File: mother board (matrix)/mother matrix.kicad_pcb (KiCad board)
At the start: 4 copper layers, 83.5 x 102.9 mm, 174 parts, among them J1 POWER, J2 DATA IN, J3 DATA OUT, J4 Serial_BUS, J5 OUTPUT, J6 INPUT, Q1 PMV45EN2R, Q10 PMV45EN2R, Q2 PMV45EN2R, Q3 PMV45EN2R, Q4 PMV45EN2R, Q5 PMV45EN2R, Q6 PMV45EN2R, Q7 PMV45EN2R, Q8 PMV45EN2R, Q9 PMV45EN2R, U1 SM16206, U2 SM16206, U3 SM16206

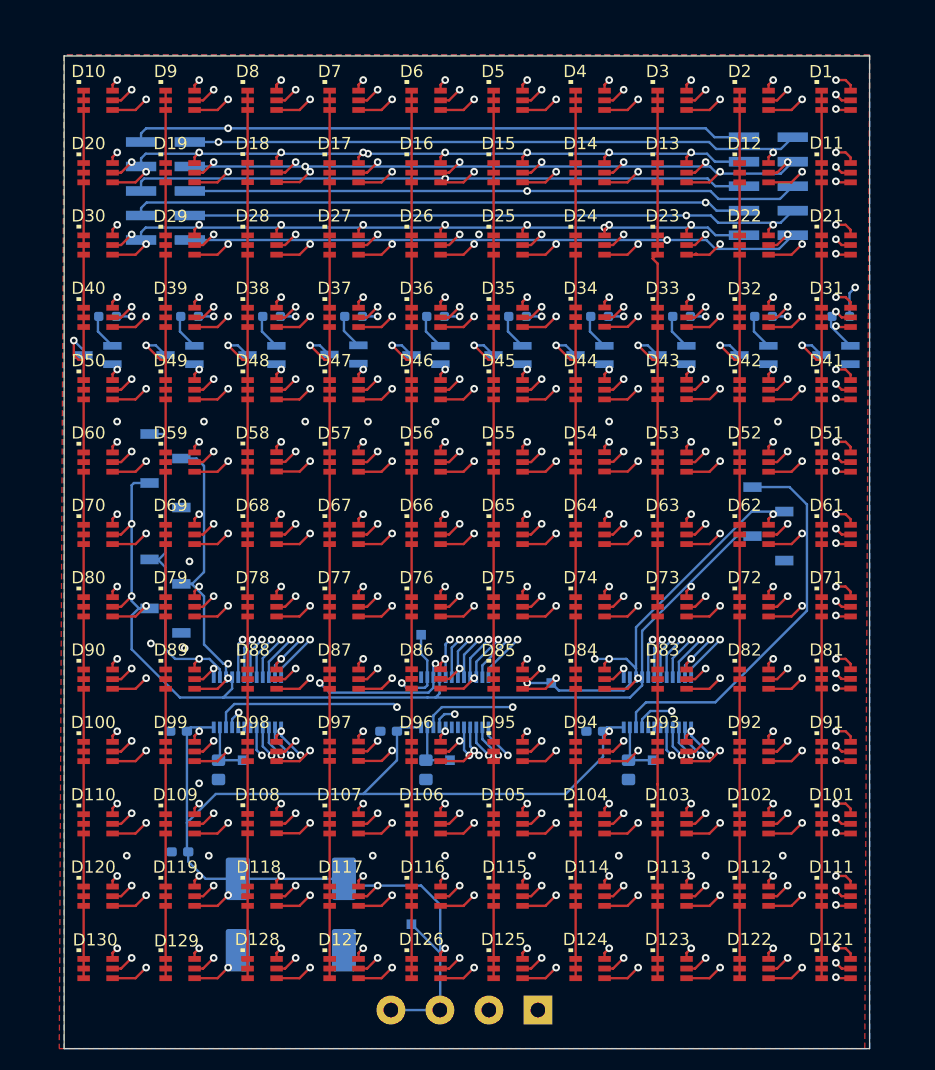
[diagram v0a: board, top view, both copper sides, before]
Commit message: Fixed GND planes and rerouted bottom layer signals
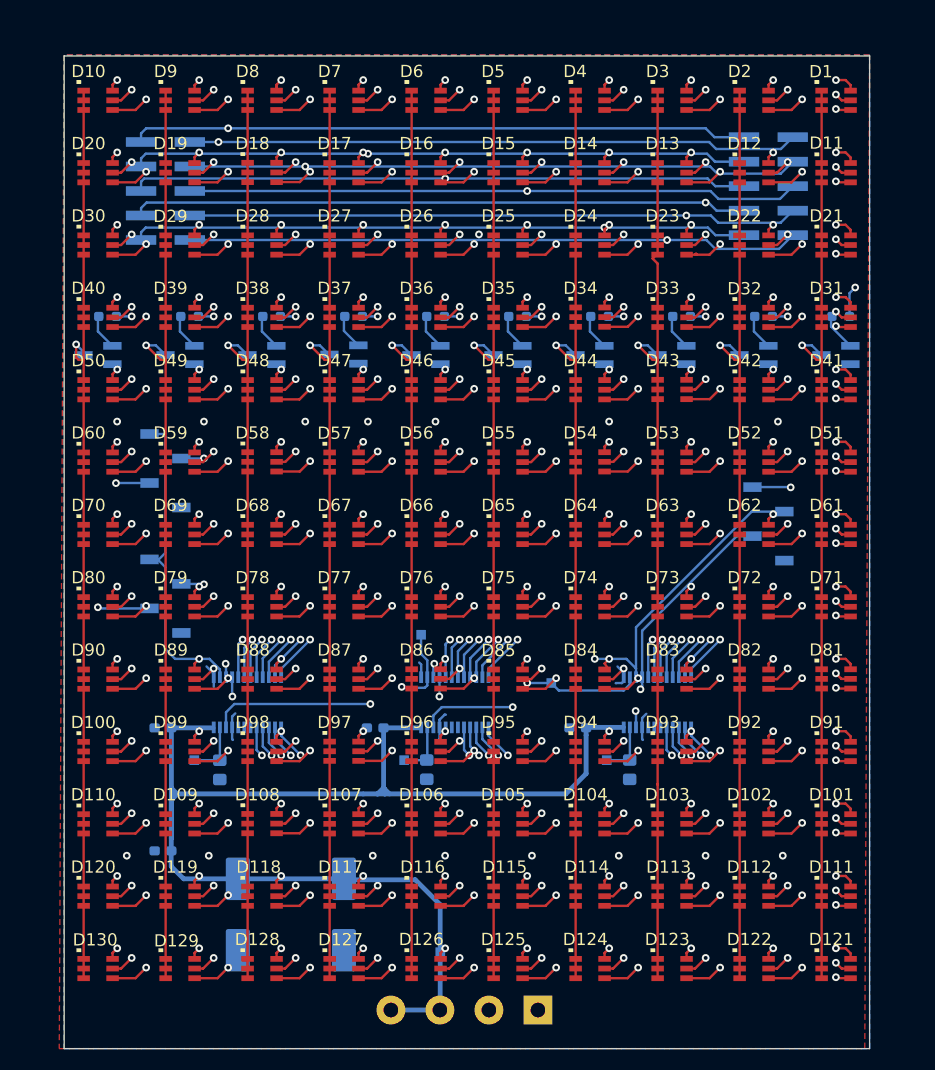
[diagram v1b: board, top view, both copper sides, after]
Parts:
- moved TP1 5.01 mm to (114.5, 106.1)
- moved TP2 4.76 mm to (136.2, 106.1)
- moved TP3 4.76 mm to (157.2, 106.1)
- moved TP4 4.17 mm to (140.0, 126.0)
- moved C4 1.79 mm to (154.2, 102.8)
- moved C6 1.76 mm to (111.2, 115.5)
- moved C2 1.66 mm to (111.2, 102.8)
- moved C3 1.44 mm to (133.2, 102.8)
- moved R1 0.13 mm to (117.1, 107.1)
- moved R3 0.12 mm to (159.6, 107.1)
- moved R2 0.09 mm to (138.6, 107.1)
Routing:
- net S_LE: track 103.2 -> 112.1 mm, vias 0 -> 5
- net +5V: track 126.8 -> 134.2 mm
- net GND: track 8.78 -> 15.6 mm, vias 22 -> 15
- net /Led/R_Row9: track 124.8 -> 121.2 mm
- net /Led/Col9: track 90.2 -> 86.7 mm
- net S_CLK: track 101.5 -> 98.5 mm, vias 4 -> 5
- net /Led/G_Row4: track 134.2 -> 131.7 mm
- net /Led/G_Row5: track 126.3 -> 124.0 mm
- net /Led/R_Row8: track 126.1 -> 124.0 mm
- net /Led/G_Row6: track 118.2 -> 116.2 mm
- net SDO: track 41.1 -> 39.3 mm, vias 0 -> 2
- net Net-(U1-SDO): track 30.5 -> 28.7 mm
- net /Led/R_Row12: track 135.7 -> 134.0 mm
- net /Led/G_Row7: track 110.0 -> 108.5 mm
- net /Led/R_Row11: track 127.9 -> 126.7 mm
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
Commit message: Changed all vias to through and modified whole layout
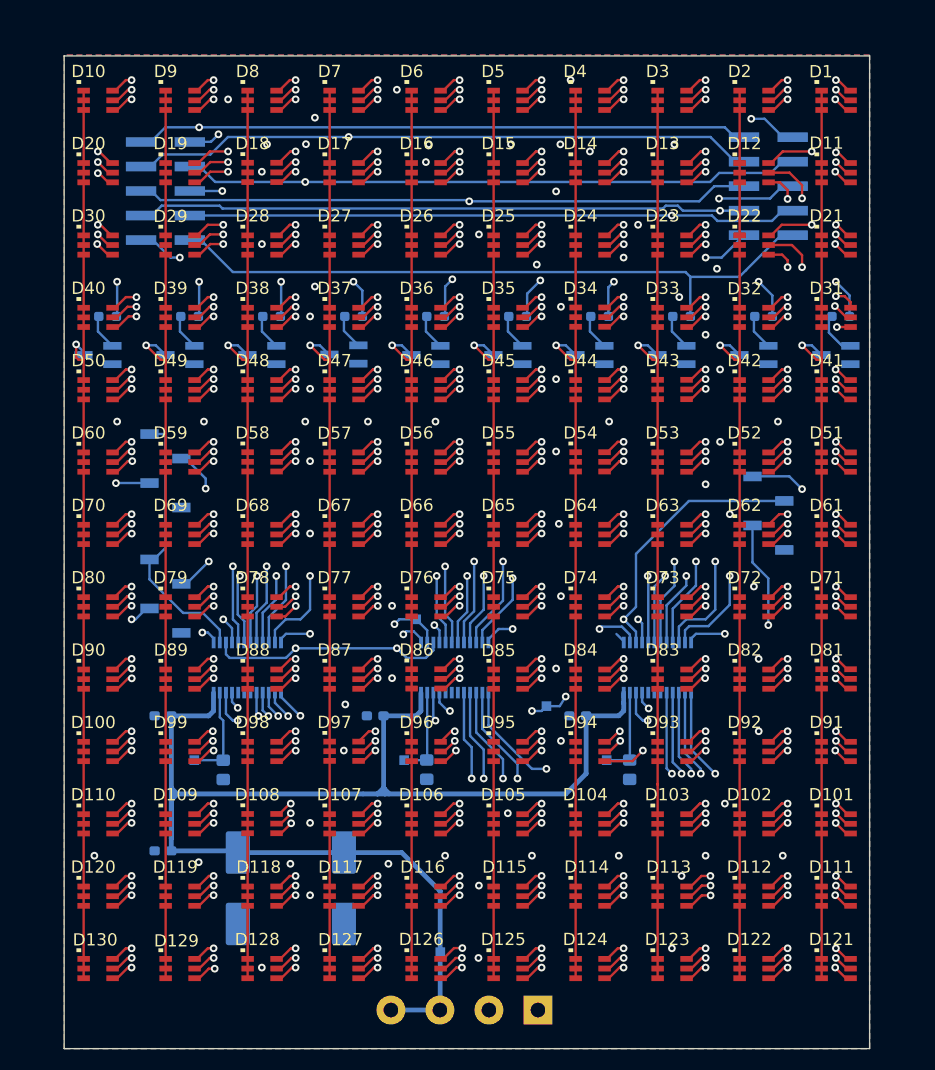
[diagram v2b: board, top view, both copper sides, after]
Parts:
- moved U1 3.60 mm to (120.0, 96.5)
- moved U2 3.60 mm to (141.5, 96.5)
- moved U3 3.60 mm to (162.5, 96.5)
- moved C1 2.72 mm to (130.0, 119.4)
- moved C5 2.72 mm to (119.0, 119.4)
- moved TP6 2.45 mm to (151.0, 100.5)
- moved TP5 1.68 mm to (137.5, 91.5)
- moved C2 1.25 mm to (111.2, 101.5)
- moved C3 1.25 mm to (133.2, 101.5)
- moved C4 1.25 mm to (154.2, 101.5)
- moved J3 1.10 mm to (174.0, 80.5)
- moved R1 0.36 mm to (117.5, 107.1)
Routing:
- net /Led/Col9: track 86.7 -> 105.8 mm, vias 2 -> 5
- net /Led/R_Row0: track 169.0 -> 154.0 mm
- net /Led/R_Row5: track 132.2 -> 117.4 mm
- net /Led/R_Row4: track 139.6 -> 125.2 mm
- net /Led/R_Row6: track 124.9 -> 110.5 mm
- net /Led/B_Row8: track 106.6 -> 120.8 mm
- net /Led/R_Row3: track 146.9 -> 132.9 mm
- net /Led/B_Row9: track 101.7 -> 115.4 mm
- net /Led/B_Row10: track 97.5 -> 111.0 mm
- net /Led/B_Row1: track 146.3 -> 158.9 mm
- net /Led/B_Row11: track 104.3 -> 116.7 mm
- net /Led/B_Row12: track 111.6 -> 123.9 mm
- net /Led/R_Row9: track 121.2 -> 109.4 mm
- net /Led/R_Row7: track 122.5 -> 110.7 mm
- net /Led/R_Row8: track 124.0 -> 112.3 mm
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
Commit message: added mounting holes,text on silk,fidducial markers,adjusted size of board
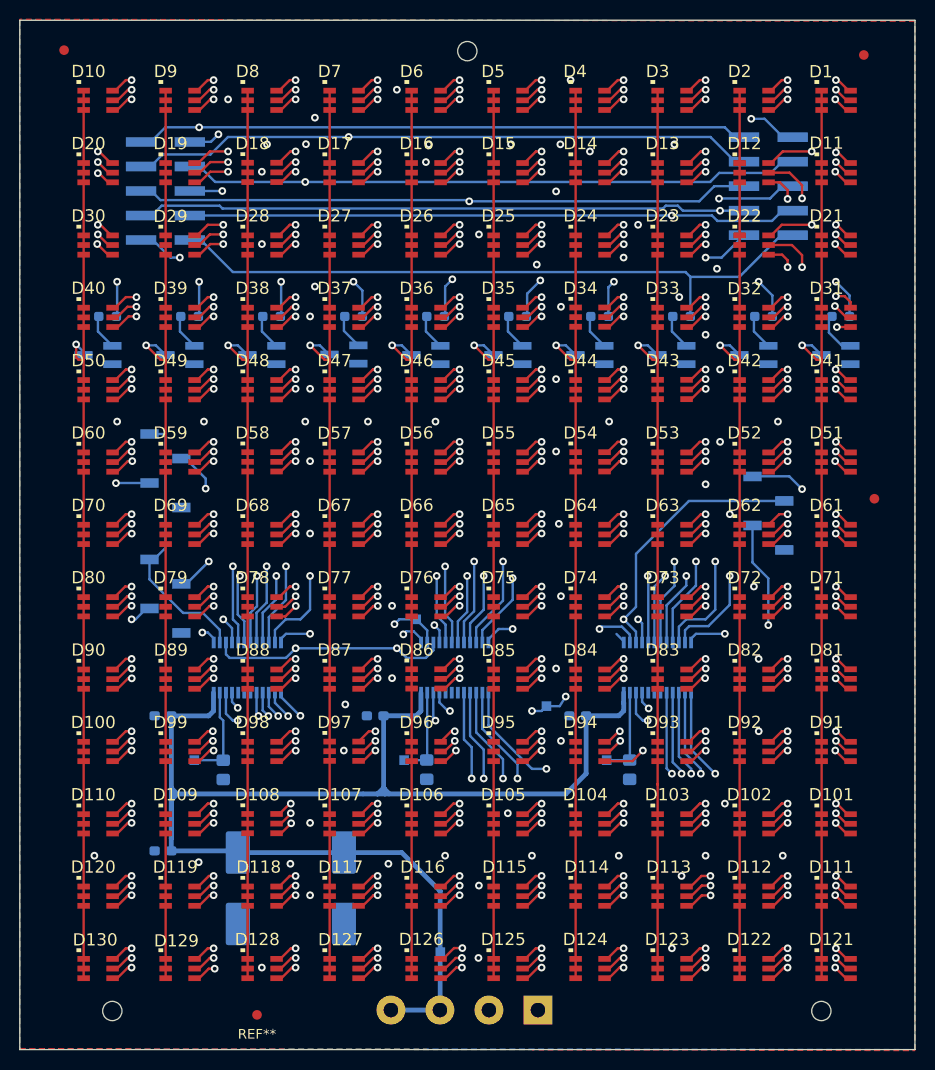
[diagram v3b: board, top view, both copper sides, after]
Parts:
- added ?: , , F.Cu at (179.5, 132.1)
- added ?: , , F.Cu at (142.8, 32.6)
- added ?: , , F.Cu at (183.9, 33.0)
- added ?: , , F.Cu at (185.0, 79.0)
- added ?: , , F.Cu at (101.0, 32.5)
- added REF**: Fiducial_1mm_Mask2mm, Fiducial:Fiducial_1mm_Mask2mm, F.Cu at (121.0, 132.5)
- added REF**: MountingHole_2mm, MountingHole:MountingHole_2mm, F.Cu at (106.0, 132.1)
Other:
- board size 83.5 x 102.9 mm -> 92.8 x 106.7 mm
- board text added: "0"
- board text added: "1"
- board text added: "2"
- board text added: "3"
- board text added: "5"
- board text added: "5V"
- board text added: "6"
- board text added: "7"
- board text added: "8"
- board text added: "9"
- board text added: "BLUE"
- board text added: "CLK"
- board text added: "DATA IN"
- board text added: "DATA OUT"
- board text added: "DI"
- board text added: "GND"
- board text added: "GREEN"
- board text added: "IN"
- board text added: "LE"
- board text added: "LED Motherboard v2.0"
- board text added: "RED"
- board text added: "SCLK"
- board text added: "SDATA"
- board text added: "SDO"
- board text added: "SLE"
